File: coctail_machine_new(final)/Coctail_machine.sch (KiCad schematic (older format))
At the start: 16 parts, among them M1 Water_pump, M2 Water_pump, M3 Water_punp, SW1 SW, SW2 SW, SW3 SW, U1 hx711

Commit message: Made base functionality
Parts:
- renumbered SW3 to SW1, SW1 to SW3
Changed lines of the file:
@@
 	3600 3700 3600 3450
 $Comp
-L Switch:SW_Push_Dual_x2 SW1
+L Switch:SW_Push_Dual_x2 SW3
 U 1 1 5FC39A88
 P 3800 4600
-F 0 "SW1" H 3800 4885 50  0000 C CNN
+F 0 "SW3" H 3800 4885 50  0000 C CNN
 F 1 "SW" H 3800 4794 50  0000 C CNN
 F 2 "" H 3800 4800 50  0001 C CNN
@@
 $EndComp
 $Comp
-L Switch:SW_Push_Dual_x2 SW3
+L Switch:SW_Push_Dual_x2 SW1
 U 1 1 5FC07EEE
 P 3800 3700
-F 0 "SW3" H 3800 3985 50  0000 C CNN
+F 0 "SW1" H 3800 3985 50  0000 C CNN
 F 1 "SW" H 3800 3894 50  0000 C CNN
 F 2 "" H 3800 3900 50  0001 C CNN

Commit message: Made changes to scheme
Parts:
- added SW? (x2): SW_Push, symbol Switch:SW_Push
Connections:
- net at A?.15 (D0/RX): now also U1.8 (DT)
- net at A?.16 (D1/TX): now also U1.9 (SCK)
- net at A?.17 (D2): no longer U1.8 (DT)
- net at A?.18 (D3): no longer U1.9 (SCK)
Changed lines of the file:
@@
 $EndComp
-Wire Wire Line
-	1900 4150 2100 4150
 Wire Wire Line
 	3200 6150 3150 6150
@@
 	2100 5850 3200 5850
 Wire Wire Line
-	2050 6000 2050 4250
-Wire Wire Line
-	2050 4250 1900 4250
-Wire Wire Line
 	2050 6000 3200 6000
 $Comp
@@
 Wire Wire Line
 	1900 3650 2450 3650
-Wire Wire Line
-	2100 4150 2100 5850
 $Comp
 L Device:R R1
@@
 Wire Wire Line
 	6100 1800 6550 1800
+$Comp
+L Switch:SW_Push SW?
+U 1 1 60268D72
+P 6100 3400
+F 0 "SW?" H 6100 3685 50  0000 C CNN
+F 1 "SW_Push" H 6100 3594 50  0000 C CNN
+F 2 "" H 6100 3600 50  0001 C CNN
+F 3 "~" H 6100 3600 50  0001 C CNN
+	1    6100 3400
+	1    0    0    -1
+$EndComp
+$Comp
+L Switch:SW_Push SW?
+U 1 1 6026C5EA
+P 6600 3500
+F 0 "SW?" H 6600 3785 50  0000 C CNN
+F 1 "SW_Push" H 6600 3694 50  0000 C CNN
+F 2 "" H 6600 3700 50  0001 C CNN
+F 3 "~" H 6600 3700 50  0001 C CNN
+	1    6600 3500
+	1    0    0    -1
+$EndComp
+Wire Wire Line
+	2100 5850 2100 4350
+Wire Wire Line
+	2100 4350 1900 4350
+Wire Wire Line
+	2050 6000 2050 4450
+Wire Wire Line
+	2050 4450 1900 4450
 $EndSCHEMATC

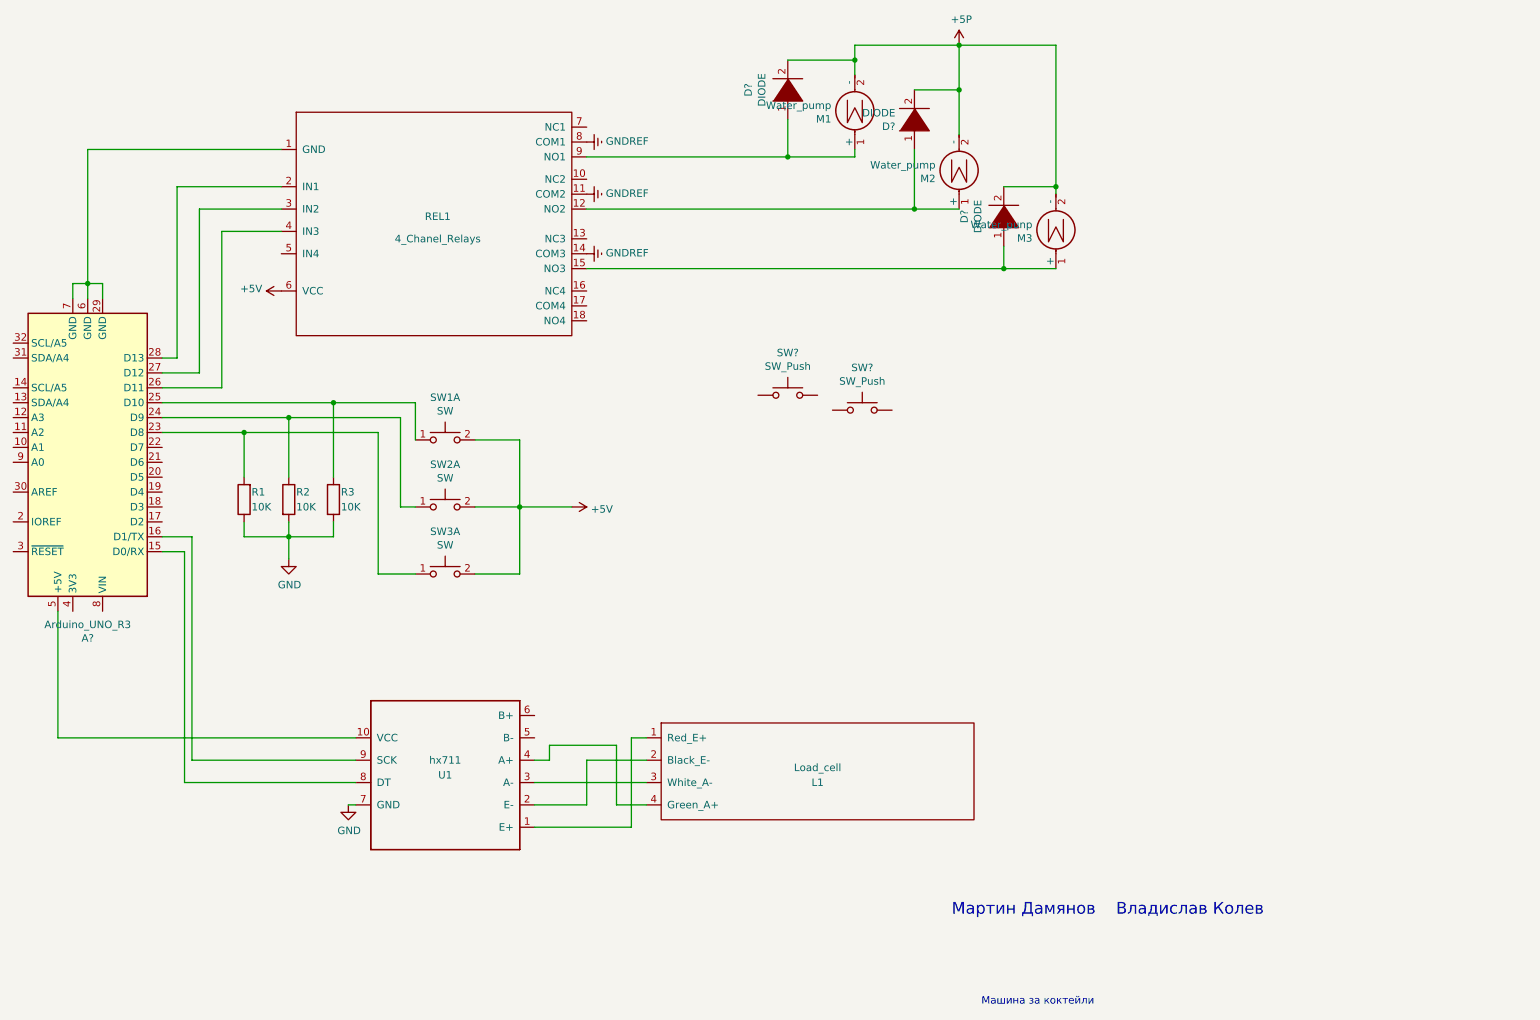
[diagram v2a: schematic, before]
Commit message: Added more buttons and display in KiCad
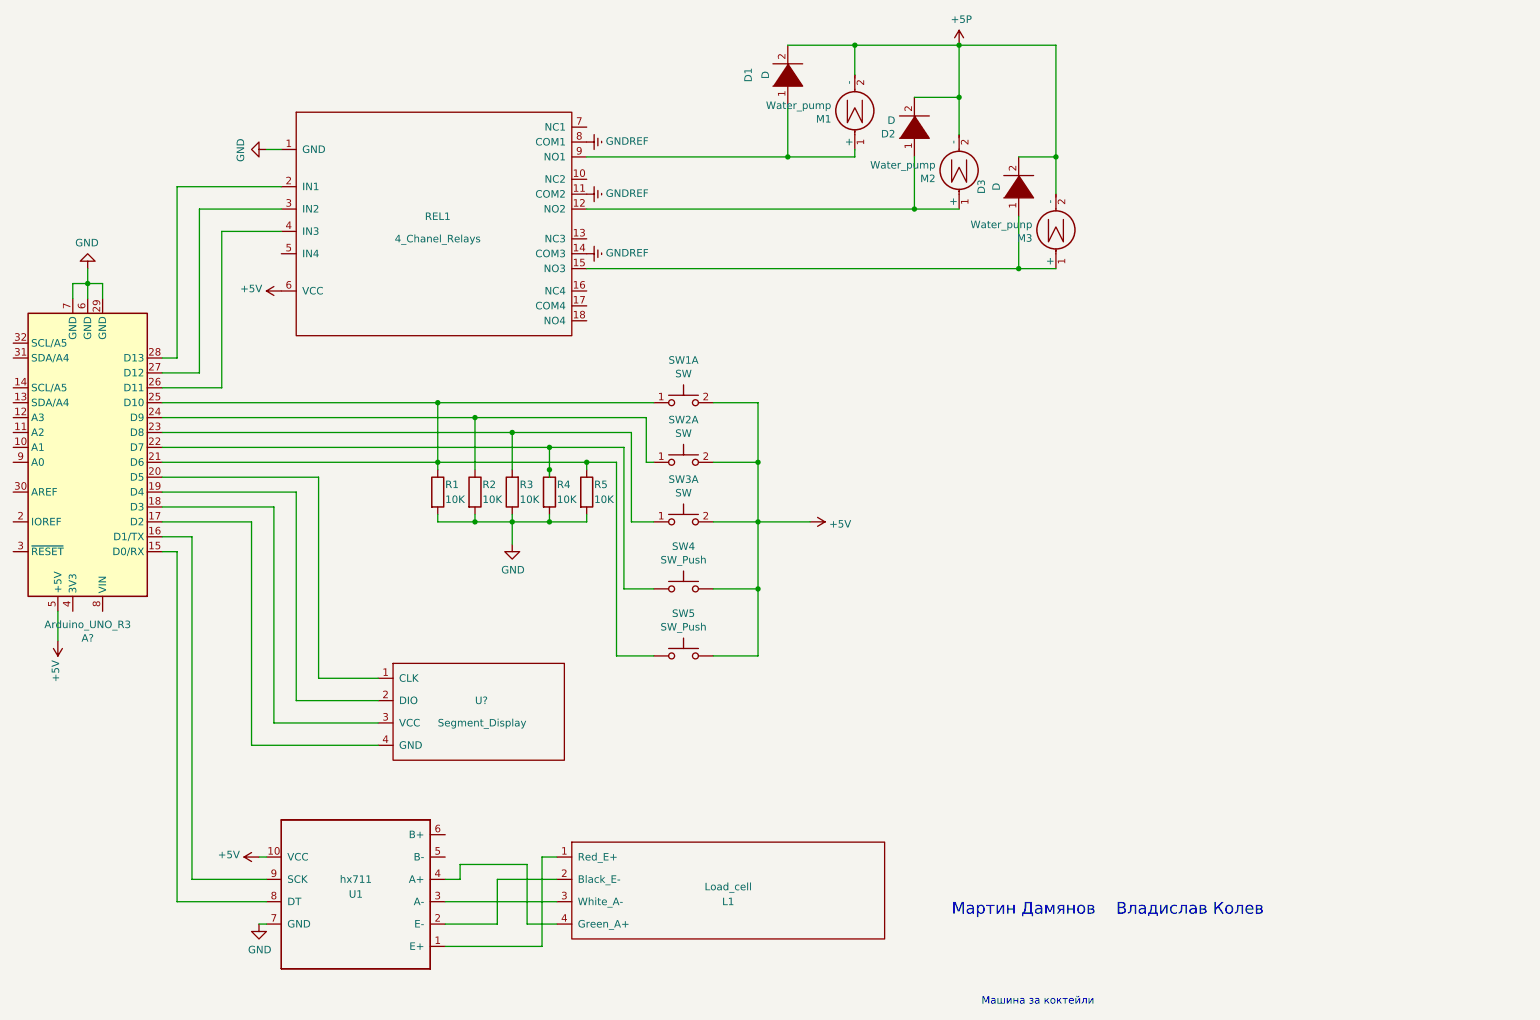
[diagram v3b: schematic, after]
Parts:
- added R1, R2: 10K, symbol Device:R
- added U?: Segment_Display, symbol Arduino:Segment_Display
- D1, D2, D3: renamed from D?; value DIODE -> D
- gave numbers to parts that had none: 2
- renumbered R1 to R3, R2 to R4, R3 to R5
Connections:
- net +5V: now also A?.5 (+5V), SW4.2, SW5.2, U1.10 (VCC)
- net GND: now also A?.29 (GND), A?.6 (GND), A?.7 (GND), REL1.1 (GND), R1.2, R2.2
- net at A?.17 (D2): now also U?.4 (GND)
- net at A?.18 (D3): now also U?.3 (VCC)
- net at A?.19 (D4): now also U?.2 (DIO)
- net at A?.20 (D5): now also U?.1 (CLK)
- net at A?.21 (D6): now also A?.25 (D10), R5.1, SW1.1 (C), SW5.1, R1.1
- net at A?.22 (D7): now also R4.1, SW4.1
- net at A?.24 (D9), SW2.1 (C): now also R2.1; no longer R4.1
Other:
- moved on the sheet: D1, D2, D3, L1, R3, R4, R5, SW1A, SW2A, SW3A, SW4, SW5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

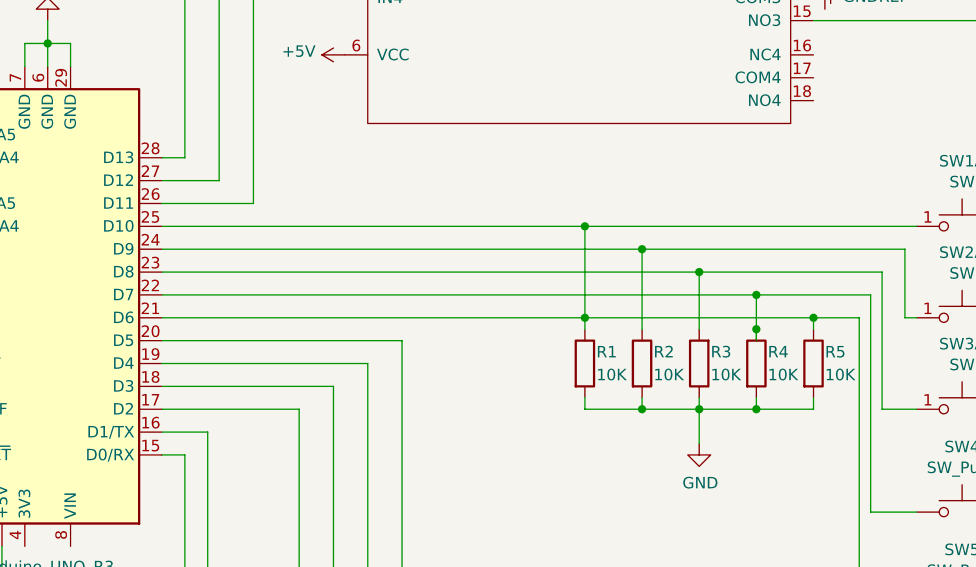
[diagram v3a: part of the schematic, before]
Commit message: Added more buttons and display in KiCad
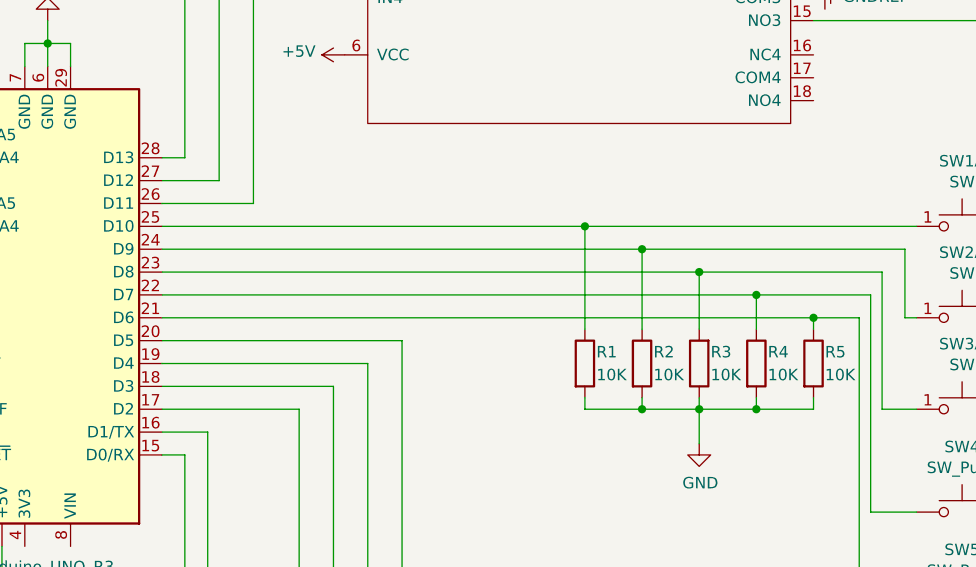
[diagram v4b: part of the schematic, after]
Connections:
- net at A?.21 (D6), R5.1, SW5.1: no longer A?.25 (D10), R1.1, SW1.1 (C)
- new net: A?.25 (D10), R1.1, SW1.1 (C)
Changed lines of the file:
@@
 	4250 3650 5050 3650
-Wire Wire Line
-	3750 3900 3750 3850
-Connection ~ 3750 3850
-Wire Wire Line
-	3750 3850 4750 3850
 Wire Wire Line
 	3750 4200 3750 4250
@@
 	4000 4250 4250 4250
 Wire Wire Line
-	3750 3450 3750 3850
-Connection ~ 3750 3450
-Wire Wire Line
 	4000 3900 4000 3550
 Connection ~ 4000 3550
 Wire Wire Line
 	4000 3550 5150 3550
-Wire Wire Line
-	4500 3750 4500 3900
-Connection ~ 4500 3750
-Wire Wire Line
-	4500 3750 5000 3750
-Connection ~ 4500 3900
-Wire Wire Line
-	4500 3900 4500 3950
-Wire Wire Line
-	3750 3450 5200 3450
 Wire Wire Line
 	4750 3900 4750 3850
@@
 	4750 3850 4950 3850
 Wire Wire Line
-	1900 3450 3750 3450
-Wire Wire Line
 	1900 3550 4000 3550
 Wire Wire Line
 	1900 3650 4250 3650
-Wire Wire Line
-	1900 3750 4500 3750
-Wire Wire Line
-	1900 3850 3750 3850
 Wire Wire Line
 	2600 6650 2100 6650
@@
 Wire Wire Line
 	1400 2650 1400 2550
+Wire Wire Line
+	1900 3450 3750 3450
+Wire Wire Line
+	1900 3850 4750 3850
+Wire Wire Line
+	1900 3750 4500 3750
+Wire Wire Line
+	3750 3900 3750 3450
+Connection ~ 3750 3450
+Wire Wire Line
+	3750 3450 5200 3450
+Wire Wire Line
+	4500 3900 4500 3750
+Connection ~ 4500 3750
+Wire Wire Line
+	4500 3750 5000 3750
 $EndSCHEMATC

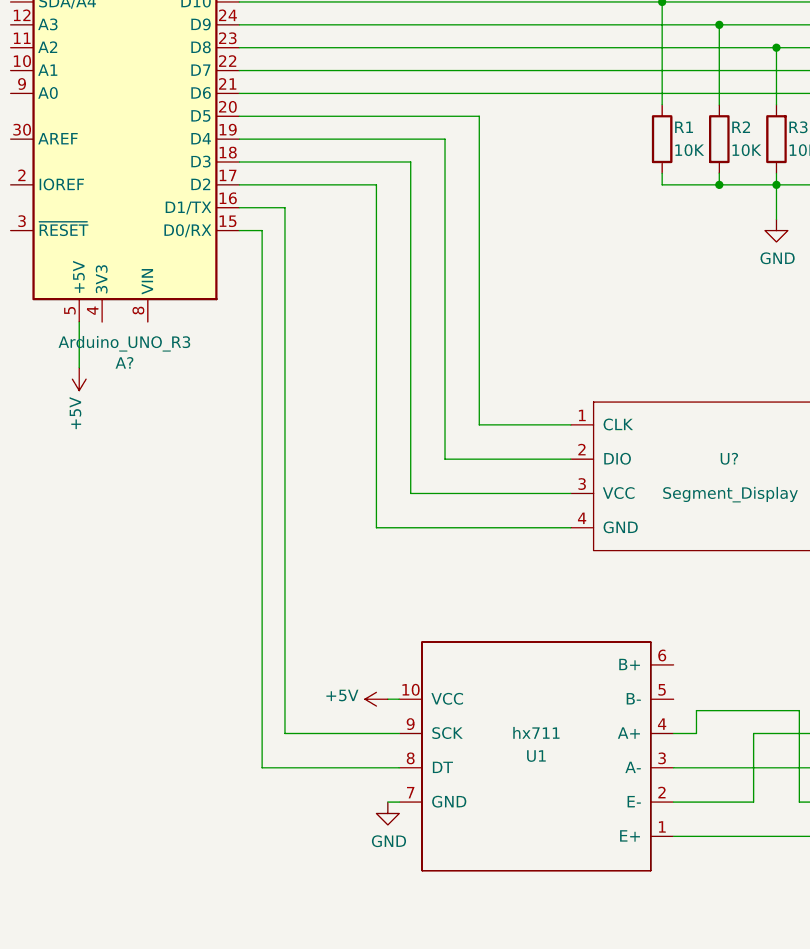
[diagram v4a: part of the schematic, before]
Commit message: Repaired scheme in KiCad
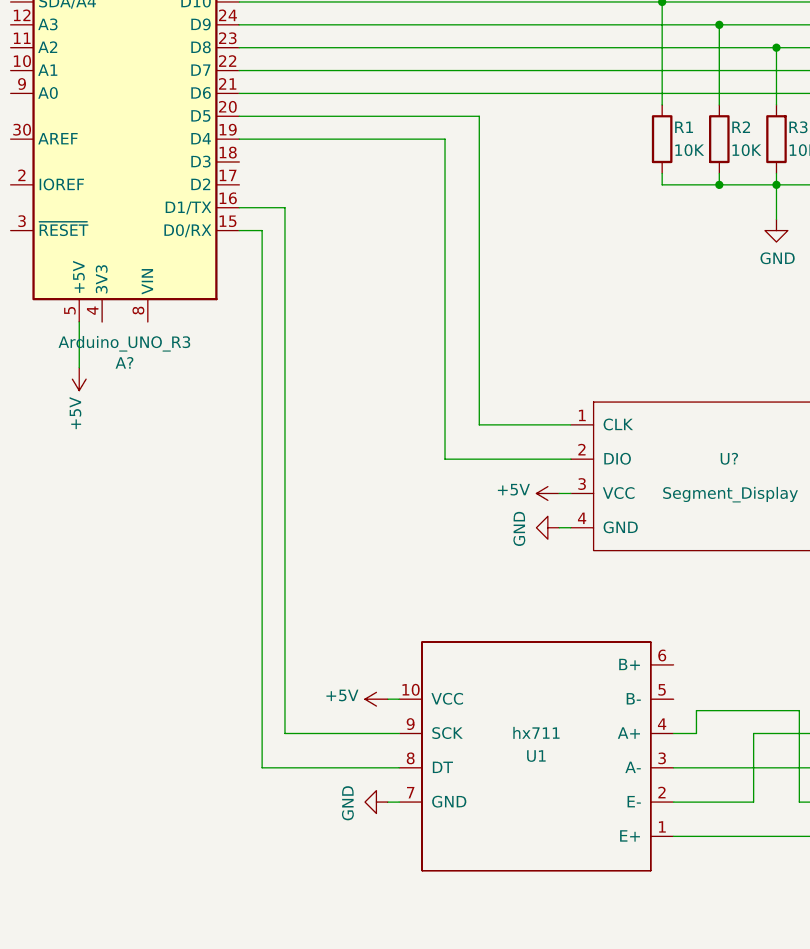
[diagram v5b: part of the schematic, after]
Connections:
- net +5V: now also U?.3 (VCC)
- net GND: now also U?.4 (GND)
- net at A?.17 (D2): no longer U?.4 (GND)
- net at A?.18 (D3): no longer U?.3 (VCC)
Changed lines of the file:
@@
 	-1   0    0    1
 $EndComp
-Wire Wire Line
-	2600 6950 2550 6950
 $Comp
 L Coctail_machine-rescue:Load_cell-Arduino-7-segment-rescue L1
@@
 F 3 "" H 2550 6950 50  0001 C CNN
 	1    2550 6950
-	1    0    0    -1
+	0    1    1    0
 $EndComp
 $Comp
@@
 	2800 5450 3350 5450
 Wire Wire Line
-	1900 4150 2650 4150
-Wire Wire Line
-	2650 4150 2650 5600
-Wire Wire Line
-	2650 5600 3350 5600
-Wire Wire Line
-	1900 4250 2500 4250
-Wire Wire Line
-	2500 4250 2500 5750
-Wire Wire Line
-	2500 5750 3350 5750
-$Comp
-L power:+5V #PWR?
-U 1 1 6039EA57
-P 2550 6500
-F 0 "#PWR?" H 2550 6350 50  0001 C CNN
-F 1 "+5V" V 2565 6628 50  0000 L CNN
-F 2 "" H 2550 6500 50  0001 C CNN
-F 3 "" H 2550 6500 50  0001 C CNN
-	1    2550 6500
-	0    -1   -1   0
-$EndComp
-Wire Wire Line
-	2550 6500 2600 6500
-Wire Wire Line
 	6550 1050 6550 1250
 Wire Wire Line
@@
 Wire Wire Line
 	4500 3750 5000 3750
+Wire Wire Line
+	2550 6500 2600 6500
+$Comp
+L power:+5V #PWR?
+U 1 1 6039EA57
+P 2550 6500
+F 0 "#PWR?" H 2550 6350 50  0001 C CNN
+F 1 "+5V" V 2565 6628 50  0000 L CNN
+F 2 "" H 2550 6500 50  0001 C CNN
+F 3 "" H 2550 6500 50  0001 C CNN
+	1    2550 6500
+	0    -1   -1   0
+$EndComp
+$Comp
+L power:+5V #PWR?
+U 1 1 602851FC
+P 3300 5600
+F 0 "#PWR?" H 3300 5450 50  0001 C CNN
+F 1 "+5V" V 3315 5728 50  0000 L CNN
+F 2 "" H 3300 5600 50  0001 C CNN
+F 3 "" H 3300 5600 50  0001 C CNN
+	1    3300 5600
+	0    -1   -1   0
+$EndComp
+Wire Wire Line
+	3300 5600 3350 5600
+Wire Wire Line
+	2550 6950 2600 6950
+$Comp
+L power:GND #PWR?
+U 1 1 6029A263
+P 3300 5750
+F 0 "#PWR?" H 3300 5500 50  0001 C CNN
+F 1 "GND" H 3305 5577 50  0000 C CNN
+F 2 "" H 3300 5750 50  0001 C CNN
+F 3 "" H 3300 5750 50  0001 C CNN
+	1    3300 5750
+	0    1    1    0
+$EndComp
+Wire Wire Line
+	3300 5750 3350 5750
 $EndSCHEMATC

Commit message: scheme update
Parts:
- added D?: DIODE, symbol pspice:DIODE
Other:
- moved on the sheet: U?
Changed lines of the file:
@@
 L Arduino:Segment_Display U?
 U 1 1 6037EFCD
-P 4100 5550
-F 0 "U?" H 4000 5650 50  0000 L CNN
-F 1 "Segment_Display" H 3750 5500 50  0000 L CNN
-F 2 "" H 4050 5550 50  0001 C CNN
-F 3 "" H 4050 5550 50  0001 C CNN
-	1    4100 5550
+P 4300 5550
+F 0 "U?" H 4200 5650 50  0000 L CNN
+F 1 "Segment_Display" H 3950 5500 50  0000 L CNN
+F 2 "" H 4250 5550 50  0001 C CNN
+F 3 "" H 4250 5550 50  0001 C CNN
+	1    4300 5550
 	1    0    0    -1
 $EndComp
-Wire Wire Line
-	3350 5300 2950 5300
 Wire Wire Line
 	2950 5300 2950 3950
@@
 Wire Wire Line
 	2800 4050 2800 5450
-Wire Wire Line
-	2800 5450 3350 5450
 Wire Wire Line
 	6550 1050 6550 1250
@@
 L power:+5V #PWR?
 U 1 1 602851FC
-P 3300 5600
-F 0 "#PWR?" H 3300 5450 50  0001 C CNN
-F 1 "+5V" V 3315 5728 50  0000 L CNN
-F 2 "" H 3300 5600 50  0001 C CNN
-F 3 "" H 3300 5600 50  0001 C CNN
-	1    3300 5600
+P 3500 5600
+F 0 "#PWR?" H 3500 5450 50  0001 C CNN
+F 1 "+5V" V 3515 5728 50  0000 L CNN
+F 2 "" H 3500 5600 50  0001 C CNN
+F 3 "" H 3500 5600 50  0001 C CNN
+	1    3500 5600
 	0    -1   -1   0
 $EndComp
 Wire Wire Line
-	3300 5600 3350 5600
+	3500 5600 3550 5600
 Wire Wire Line
 	2550 6950 2600 6950
@@
 L power:GND #PWR?
 U 1 1 6029A263
-P 3300 5750
-F 0 "#PWR?" H 3300 5500 50  0001 C CNN
-F 1 "GND" H 3305 5577 50  0000 C CNN
-F 2 "" H 3300 5750 50  0001 C CNN
-F 3 "" H 3300 5750 50  0001 C CNN
-	1    3300 5750
+P 3500 5750
+F 0 "#PWR?" H 3500 5500 50  0001 C CNN
+F 1 "GND" H 3505 5577 50  0000 C CNN
+F 2 "" H 3500 5750 50  0001 C CNN
+F 3 "" H 3500 5750 50  0001 C CNN
+	1    3500 5750
 	0    1    1    0
 $EndComp
 Wire Wire Line
-	3300 5750 3350 5750
+	3500 5750 3550 5750
+Wire Wire Line
+	2950 5300 3550 5300
+Wire Wire Line
+	2800 5450 3550 5450
+$Comp
+L pspice:DIODE D?
+U 1 1 60309455
+P 9700 1400
+F 0 "D?" H 9700 1665 50  0000 C CNN
+F 1 "DIODE" H 9700 1574 50  0000 C CNN
+F 2 "" H 9700 1400 50  0001 C CNN
+F 3 "~" H 9700 1400 50  0001 C CNN
+	1    9700 1400
+	1    0    0    -1
+$EndComp
 $EndSCHEMATC

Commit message: Fixed sheme
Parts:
- removed D?: DIODE, symbol pspice:DIODE
- U?: symbol Arduino:Segment_Display -> Coctail_machine-rescue:Segment_Display-Arduino
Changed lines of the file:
@@
 	2000 6800 2600 6800
 $Comp
-L Arduino:Segment_Display U?
+L Coctail_machine-rescue:Segment_Display-Arduino U?
 U 1 1 6037EFCD
 P 4300 5550
@@
 Wire Wire Line
 	2800 5450 3550 5450
-$Comp
-L pspice:DIODE D?
-U 1 1 60309455
-P 9700 1400
-F 0 "D?" H 9700 1665 50  0000 C CNN
-F 1 "DIODE" H 9700 1574 50  0000 C CNN
-F 2 "" H 9700 1400 50  0001 C CNN
-F 3 "~" H 9700 1400 50  0001 C CNN
-	1    9700 1400
-	1    0    0    -1
-$EndComp
 $EndSCHEMATC
